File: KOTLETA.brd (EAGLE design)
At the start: 27 x 40.2 mm, 126 parts, among them CON1 CON-6P, CON2 CON-4P-JST_GH-RA, CON3 CON-4P-JST_GH-RA, IC1 STM32F105RCT6, IC2 CAT24C02, IC3 SN65HVD232D, IC4 LMR14010ADDCT, IC5 LM75BD-TSSOP8, IC6 FAN7888, IC7 ZXCT1051, IC8 3.3V, Q1 CSD18510Q5B, Q2 CSD18510Q5B, Q3 CSD18510Q5B, Q4 CSD18510Q5B, Q5 CSD18510Q5B, Q6 CSD18510Q5B, X1 24MHz

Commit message: BOM updates
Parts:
- C24, C30, C32: value 2.2nF -> 1800pF
- R13, R18, R22: value 3K9 -> 4K7
- moved PAD3 0.20 mm to (0.00, 18.7)
- moved PAD5 0.20 mm to (0.00, 16.1)
- moved PAD1 0.20 mm to (0.00, 20.5)
- moved PAD2 0.20 mm to (0.00, 19.6)
- moved PAD4 0.20 mm to (0.00, 15.2)
- moved PAD6 0.20 mm to (0.00, 17.1)

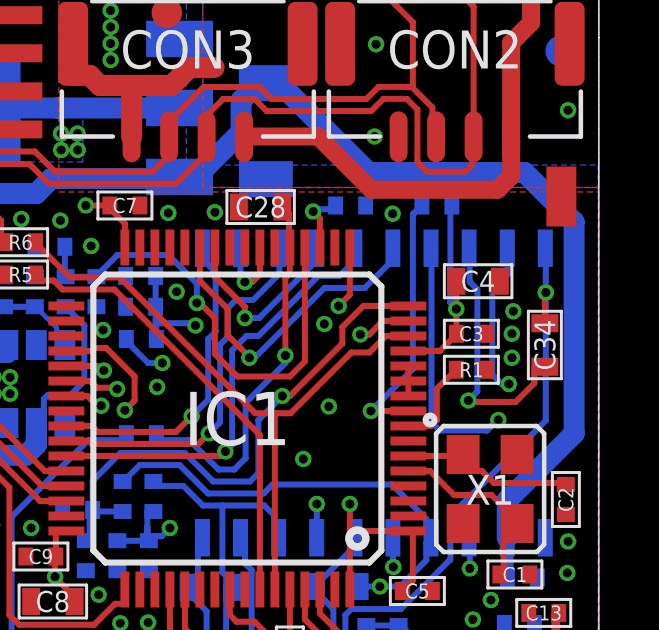
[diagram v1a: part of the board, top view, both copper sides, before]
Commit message: Its 10V5 noew. HW ID stuff also fixed
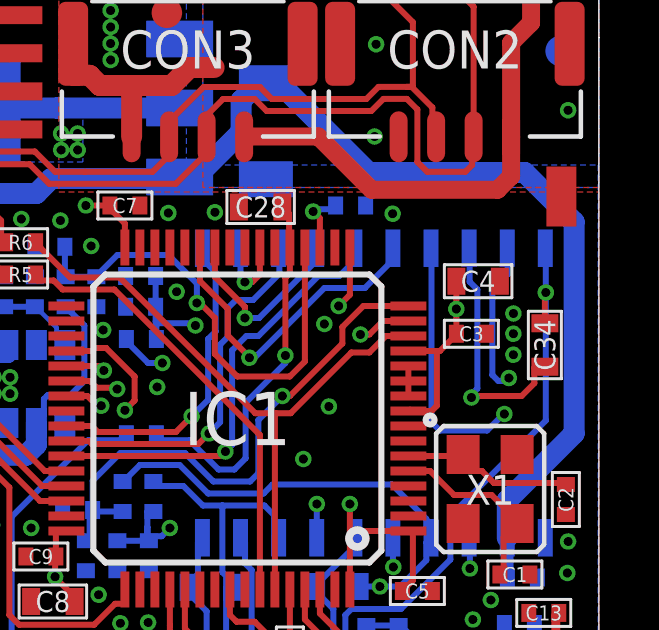
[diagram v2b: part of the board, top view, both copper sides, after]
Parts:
- removed R1, R29: 200R, R_digikey:R0402
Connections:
- removed net N$15: IC1.9, R29.1
- removed net N$9: IC1.8, R1.1
- net GND: now also IC1.8; no longer R1.2
- net VDD_3V3: now also IC1.9; no longer R29.2
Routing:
- net N$15: track 8.87 -> 0.00 mm, vias 1 -> 0
- net N$9: track 2.98 -> 0.00 mm
- net VDD_3V3: track 57.6 -> 56.9 mm

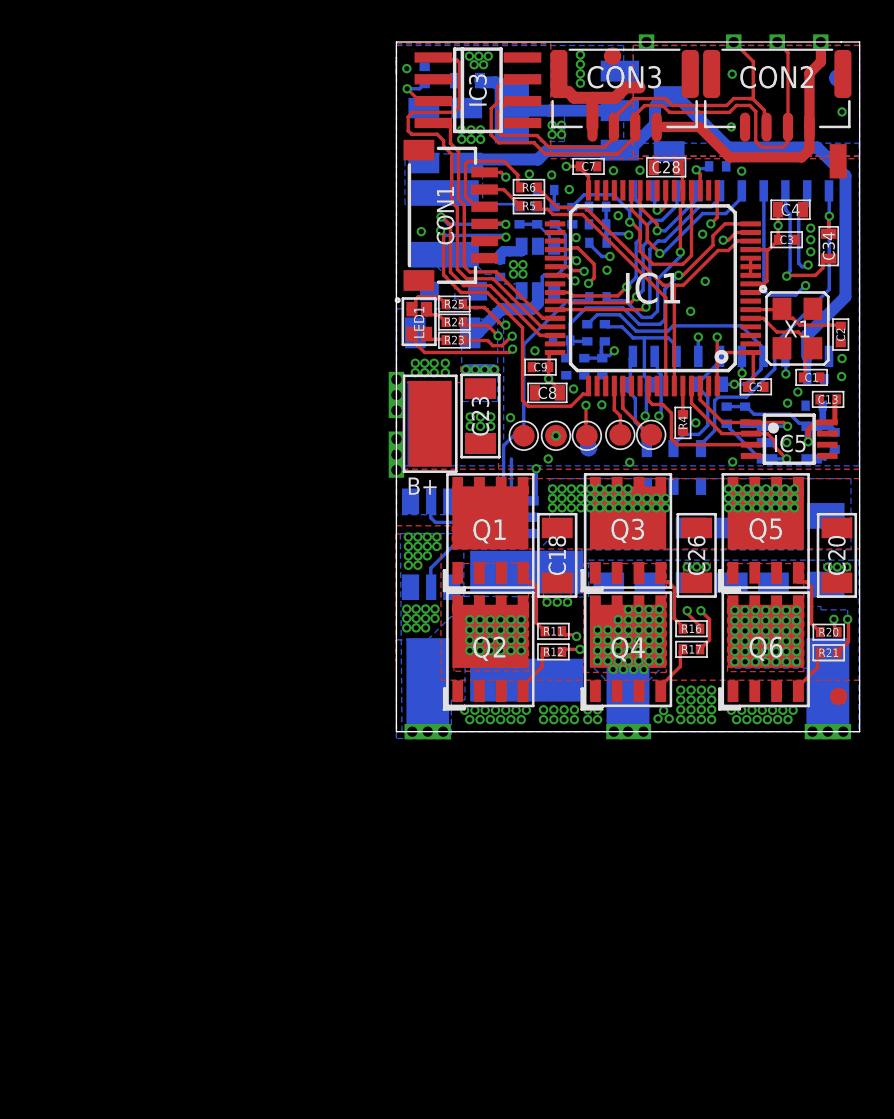
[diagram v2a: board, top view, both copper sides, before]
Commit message: pads for bulk capacitor
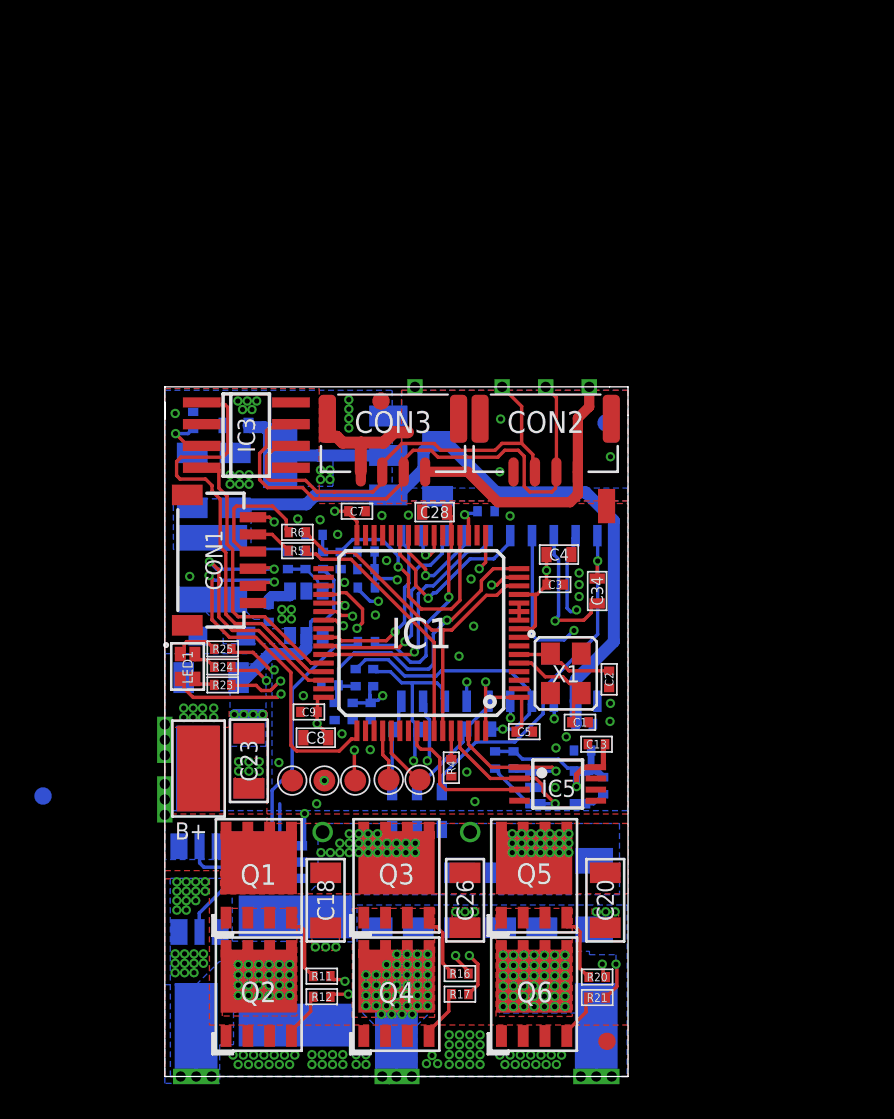
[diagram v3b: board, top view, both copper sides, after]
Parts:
- added PAD21, PAD22: PAD-HOLE-0.8, PADS:HOLE_0.8
- moved FD4 37.7 mm to (-20.6, -3.75)
- moved D5 25.1 mm to (2.65, -4.60)
- moved D4 25.0 mm to (1.20, -4.60)
- moved D3 24.9 mm to (-0.25, -4.60)
- moved C10 24.2 mm to (10.8, -1.10)
- moved C21 24.2 mm to (8.47, -9.82)
- moved C4 24.2 mm to (9.47, 10.3)
- moved C6 24.2 mm to (5.22, 12.8)
- moved FD3 24.2 mm to (12.2, 18.0)
- moved A 24.2 mm to (-11.7, -17.1)
- moved B 24.2 mm to (0.00, -17.1)
- moved B+ 24.2 mm to (-11.5, -2.15)
- moved B- 24.2 mm to (-11.6, -2.15)
- moved C1 24.2 mm to (10.7, 0.55)
- moved C11 24.2 mm to (-11.8, 18.1)
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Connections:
- net GND: now also PAD22.P$1
- net VBAT: now also PAD21.P$1
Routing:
- net FET_C_VB: track 20.1 -> 21.2 mm
- net FET_A_HO: track 22.3 -> 21.4 mm
- net FET_A_VS: track 27.9 -> 27.0 mm
- net VBAT: track 14.5 -> 15.4 mm, vias 63 -> 49
- net N$20: track 5.04 -> 5.66 mm
- net FET_A_VB: track 6.09 -> 5.50 mm
- net GND: vias 63 -> 62

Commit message: blah
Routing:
- net FET_B_VS: vias 42 -> 38
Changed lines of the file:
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@@
 <grid distance="0.025" unitdist="mm" unit="mm" style="lines" multiple="2" display="yes" altdistance="1" altunitdist="mm" altunit="mm"/>
 <layers>
-<layer number="1" name="Top" color="4" fill="1" visible="yes" active="yes"/>
+<layer number="1" name="Top" color="4" fill="1" visible="no" active="yes"/>
 <layer number="2" name="gnd" color="1" fill="3" visible="no" active="yes"/>
 <layer number="3" name="SUPPLY" color="2" fill="5" visible="no" active="yes"/>
@@
 <layer number="17" name="Pads" color="2" fill="1" visible="yes" active="yes"/>
 <layer number="18" name="Vias" color="2" fill="1" visible="yes" active="yes"/>
-<layer number="19" name="Unrouted" color="14" fill="1" visible="no" active="yes"/>
+<layer number="19" name="Unrouted" color="14" fill="1" visible="yes" active="yes"/>
 <layer number="20" name="Dimension" color="15" fill="1" visible="yes" active="yes"/>
-<layer number="21" name="tPlace" color="7" fill="1" visible="yes" active="yes"/>
+<layer number="21" name="tPlace" color="7" fill="1" visible="no" active="yes"/>
 <layer number="22" name="bPlace" color="7" fill="1" visible="no" active="yes"/>
-<layer number="23" name="tOrigins" color="15" fill="1" visible="yes" active="yes"/>
+<layer number="23" name="tOrigins" color="15" fill="1" visible="no" active="yes"/>
 <layer number="24" name="bOrigins" color="15" fill="1" visible="no" active="yes"/>
-<layer number="25" name="tNames" color="7" fill="1" visible="yes" active="yes"/>
+<layer number="25" name="tNames" color="7" fill="1" visible="no" active="yes"/>
 <layer number="26" name="bNames" color="7" fill="1" visible="no" active="yes"/>
 <layer number="27" name="tValues" color="7" fill="1" visible="no" active="yes"/>
@@
 <layer number="49" name="Reference" color="7" fill="1" visible="no" active="yes"/>
 <layer number="50" name="dxf" color="7" fill="1" visible="no" active="no"/>
-<layer number="51" name="tDocu" color="7" fill="1" visible="yes" active="yes"/>
+<layer number="51" name="tDocu" color="7" fill="1" visible="no" active="yes"/>
 <layer number="52" name="bDocu" color="7" fill="1" visible="no" active="yes"/>
 <layer number="53" name="tGND_GNDA" color="7" fill="9" visible="no" active="no"/>
@@
 <via x="1.8" y="-1.7" extent="1-16" drill="0.3"/>
 <wire x1="1.8" y1="-1.7" x2="1.925" y2="-1.575" width="0.2" layer="16"/>
-<wire x1="2.15" y1="-8.55" x2="2.15" y2="-2.325" width="0.2" layer="3"/>
-<wire x1="2.15" y1="-2.325" x2="1.8" y2="-1.975" width="0.2" layer="3"/>
-<wire x1="1.8" y1="-1.975" x2="1.8" y2="-1.7" width="0.2" layer="3"/>
-<wire x1="-1.9" y1="-9.85" x2="0.85" y2="-9.85" width="0.2" layer="3"/>
-<wire x1="0.85" y1="-9.85" x2="2.15" y2="-8.55" width="0.2" layer="3"/>
+<wire x1="2.3" y1="-8.05" x2="2.3" y2="-2.225" width="0.2" layer="3"/>
+<wire x1="2.3" y1="-2.225" x2="1.8" y2="-1.725" width="0.2" layer="3"/>
+<wire x1="1.8" y1="-1.725" x2="1.8" y2="-1.7" width="0.2" layer="3"/>
+<wire x1="-1.975" y1="-9.925" x2="0.425" y2="-9.925" width="0.2" layer="3"/>
+<wire x1="0.425" y1="-9.925" x2="2.3" y2="-8.05" width="0.2" layer="3"/>
 <wire x1="-3.85" y1="-14.25" x2="-3.65" y2="-14.45" width="0.2" layer="1"/>
-<wire x1="-1.9" y1="-9.85" x2="-2.8" y2="-10.75" width="0.2" layer="3"/>
-<wire x1="-2.8" y1="-10.75" x2="-2.8" y2="-14.35" width="0.2" layer="3"/>
-<wire x1="-2.8" y1="-14.35" x2="-3" y2="-14.55" width="0.2" layer="3"/>
+<wire x1="-1.975" y1="-9.925" x2="-2.95" y2="-10.9" width="0.2" layer="3"/>
+<wire x1="-2.95" y1="-10.9" x2="-2.95" y2="-14.5" width="0.2" layer="3"/>
+<wire x1="-2.95" y1="-14.5" x2="-3" y2="-14.55" width="0.2" layer="3"/>
 <wire x1="1.705" y1="1.624" x2="1.555" y2="1.774" width="0.2" layer="16"/>
 <wire x1="1.705" y1="1.624" x2="1.705" y2="0.92" width="0.2" layer="16"/>
@@
 <via x="-6.225" y="-15.375" extent="1-16" drill="0.3"/>
 <wire x1="0.95" y1="2.85" x2="2.35" y2="2.85" width="0.2" layer="16"/>
-<wire x1="1.725" y1="-8.375" x2="1.725" y2="-2.725" width="0.2" layer="3"/>
-<wire x1="1.725" y1="-2.725" x2="1" y2="-2" width="0.2" layer="3"/>
-<wire x1="1" y1="-2" x2="1" y2="-1.7" width="0.2" layer="3"/>
+<wire x1="1.725" y1="-7.825" x2="1.725" y2="-2.5" width="0.2" layer="3"/>
+<wire x1="1.725" y1="-2.5" x2="1" y2="-1.775" width="0.2" layer="3"/>
+<wire x1="1" y1="-1.775" x2="1" y2="-1.7" width="0.2" layer="3"/>
 <via x="1" y="-1.7" extent="1-16" drill="0.3"/>
 <wire x1="1.075" y1="0.125" x2="1.075" y2="-1.625" width="0.2" layer="16"/>
@@
 <vertex x="-9.4" y="-16.3"/>
 </polygon>
-<wire x1="1.725" y1="-8.375" x2="0.7" y2="-9.4" width="0.2" layer="3"/>
-<wire x1="0.7" y1="-9.4" x2="-3.6" y2="-9.4" width="0.2" layer="3"/>
+<wire x1="1.725" y1="-7.825" x2="0.15" y2="-9.4" width="0.2" layer="3"/>
+<wire x1="0.15" y1="-9.4" x2="-3.6" y2="-9.4" width="0.2" layer="3"/>
 <wire x1="-3.6" y1="-9.4" x2="-4.35" y2="-10.15" width="0.2" layer="3"/>
 <contactref element="Q2" pad="PAD_D"/>
@@
 <via x="-2.8" y="-15.3" extent="1-16" drill="0.3"/>
 <via x="4.1" y="2.9" extent="1-16" drill="0.3"/>
-<wire x1="2.925" y1="-8.375" x2="2.925" y2="1.725" width="0.2" layer="3"/>
-<wire x1="2.925" y1="1.725" x2="4.1" y2="2.9" width="0.2" layer="3"/>
-<wire x1="2.925" y1="-8.375" x2="1.05" y2="-10.25" width="0.2" layer="3"/>
-<wire x1="1.05" y1="-10.25" x2="-1.7" y2="-10.25" width="0.2" layer="3"/>
-<wire x1="-1.7" y1="-10.25" x2="-2.4" y2="-10.95" width="0.2" layer="3"/>
-<wire x1="-2.4" y1="-10.95" x2="-2.4" y2="-14.9" width="0.2" layer="3"/>
+<wire x1="2.825" y1="-8.325" x2="2.825" y2="1.625" width="0.2" layer="3"/>
+<wire x1="2.825" y1="1.625" x2="4.1" y2="2.9" width="0.2" layer="3"/>
+<wire x1="2.825" y1="-8.325" x2="0.725" y2="-10.425" width="0.2" layer="3"/>
+<wire x1="0.725" y1="-10.425" x2="-1.475" y2="-10.425" width="0.2" layer="3"/>
+<wire x1="-1.475" y1="-10.425" x2="-2.4" y2="-11.35" width="0.2" layer="3"/>
+<wire x1="-2.4" y1="-11.35" x2="-2.4" y2="-14.9" width="0.2" layer="3"/>
 <wire x1="-2.4" y1="-14.9" x2="-2.8" y2="-15.3" width="0.2" layer="3"/>
 <wire x1="-2.8" y1="-15.3" x2="-3.7" y2="-15.3" width="0.2" layer="1"/>
@@
 <via x="0.625" y="-15.975" extent="1-16" drill="0.3"/>
 <via x="1.225" y="-15.975" extent="1-16" drill="0.3"/>
-<via x="-0.875" y="-16.475" extent="1-16" drill="0.3"/>
-<via x="-0.275" y="-16.475" extent="1-16" drill="0.3"/>
-<via x="0.325" y="-16.475" extent="1-16" drill="0.3"/>
-<via x="0.925" y="-16.475" extent="1-16" drill="0.3"/>
 <wire x1="7.75066875" y1="1.92833125" x2="7.75066875" y2="2.39933125" width="0.2" layer="16"/>
 <wire x1="7.75066875" y1="1.92833125" x2="7.905" y2="1.774" width="0.2" layer="16"/>
@@
 <wire x1="8.55" y1="2.5" x2="11.731" y2="5.681" width="0.2" layer="16"/>
 <wire x1="2.65" y1="-3.5" x2="2.75" y2="-3.6" width="0.2" layer="16"/>
-<wire x1="6.9" y1="-0.6" x2="4.636825" y2="-0.6" width="0.2" layer="16"/>
+<wire x1="6.9" y1="-0.6" x2="5.025" y2="-0.6" width="0.2" layer="16"/>
+<wire x1="5.025" y1="-0.6" x2="4.911825" y2="-0.6" width="0.2" layer="16"/>
 <wire x1="6.9" y1="-0.6" x2="8.55" y2="1.05" width="0.2" layer="16"/>
 <wire x1="11.7" y1="8.925" x2="11.7" y2="9.919" width="0.2" layer="1"/>
@@
 <wire x1="11.731" y1="9.95" x2="11.731" y2="11.41" width="0.2" layer="16"/>
 <wire x1="11.731" y1="11.41" x2="11.715" y2="11.426" width="0.2" layer="16"/>
-<wire x1="4.636825" y1="-0.6" x2="2.65" y2="-2.586825" width="0.2" layer="16"/>
-<wire x1="2.65" y1="-2.586825" x2="2.65" y2="-3.5" width="0.2" layer="16"/>
+<wire x1="2.85" y1="-3.3" x2="2.85" y2="-2.661825" width="0.2" layer="16"/>
+<wire x1="2.85" y1="-3.3" x2="2.65" y2="-3.5" width="0.2" layer="16"/>
+<wire x1="2.85" y1="-2.661825" x2="4.911825" y2="-0.6" width="0.2" layer="16"/>
+<wire x1="4.911825" y1="-0.6" x2="5.025" y2="-0.6" width="0.2" layer="16"/>
 </signal>
 <signal name="USART1_TX">
@@
 <wire x1="7.15" y1="4.5" x2="8.925" y2="4.5" width="0.2" layer="1"/>
 <wire x1="8.925" y1="4.5" x2="8.975" y2="4.55" width="0.2" layer="1"/>
-<wire x1="12.4" y1="3.55" x2="12.35" y2="3.6" width="0.2" layer="1"/>
 <wire x1="12.4" y1="3.55" x2="10.0632375" y2="3.55" width="0.2" layer="1"/>
 <wire x1="10.0632375" y1="3.55" x2="9.6132375" y2="4" width="0.2" layer="1"/>

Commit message: notes
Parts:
- removed PAD21, PAD22: PAD-HOLE-0.8, PADS:HOLE_0.8
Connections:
- net GND: no longer PAD22.P$1
- net VBAT: no longer PAD21.P$1
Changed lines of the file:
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@@
 <grid distance="0.025" unitdist="mm" unit="mm" style="lines" multiple="2" display="yes" altdistance="1" altunitdist="mm" altunit="mm"/>
 <layers>
-<layer number="1" name="Top" color="4" fill="1" visible="no" active="yes"/>
+<layer number="1" name="Top" color="4" fill="1" visible="yes" active="yes"/>
 <layer number="2" name="gnd" color="1" fill="3" visible="no" active="yes"/>
 <layer number="3" name="SUPPLY" color="2" fill="5" visible="no" active="yes"/>
@@
 <layer number="19" name="Unrouted" color="14" fill="1" visible="yes" active="yes"/>
 <layer number="20" name="Dimension" color="15" fill="1" visible="yes" active="yes"/>
-<layer number="21" name="tPlace" color="7" fill="1" visible="no" active="yes"/>
+<layer number="21" name="tPlace" color="7" fill="1" visible="yes" active="yes"/>
 <layer number="22" name="bPlace" color="7" fill="1" visible="no" active="yes"/>
-<layer number="23" name="tOrigins" color="15" fill="1" visible="no" active="yes"/>
+<layer number="23" name="tOrigins" color="15" fill="1" visible="yes" active="yes"/>
 <layer number="24" name="bOrigins" color="15" fill="1" visible="no" active="yes"/>
-<layer number="25" name="tNames" color="7" fill="1" visible="no" active="yes"/>
+<layer number="25" name="tNames" color="7" fill="1" visible="yes" active="yes"/>
 <layer number="26" name="bNames" color="7" fill="1" visible="no" active="yes"/>
 <layer number="27" name="tValues" color="7" fill="1" visible="no" active="yes"/>
@@
 <layer number="49" name="Reference" color="7" fill="1" visible="no" active="yes"/>
 <layer number="50" name="dxf" color="7" fill="1" visible="no" active="no"/>
-<layer number="51" name="tDocu" color="7" fill="1" visible="no" active="yes"/>
+<layer number="51" name="tDocu" color="7" fill="1" visible="yes" active="yes"/>
 <layer number="52" name="bDocu" color="7" fill="1" visible="no" active="yes"/>
 <layer number="53" name="tGND_GNDA" color="7" fill="9" visible="no" active="no"/>
@@
 <attribute name="VALUE" x="-6.2" y="9.975" size="0.5" layer="28" font="vector" ratio="15" rot="MR270" align="center"/>
 </element>
-<element name="PAD21" library="PADS" library_urn="urn:adsk.eagle:library:3188696" package="HOLE_0.8" value="PAD-HOLE-0.8" x="4.3" y="-5.85" smashed="yes" rot="MR90"/>
-<element name="PAD22" library="PADS" library_urn="urn:adsk.eagle:library:3188696" package="HOLE_0.8" value="PAD-HOLE-0.8" x="-4.3" y="-5.85" smashed="yes" rot="R90"/>
 </elements>
 <signals>
@@
 </polygon>
 <wire x1="-13.5" y1="0.425" x2="-13.5" y2="-0.475" width="0.2" layer="1"/>
-<contactref element="PAD21" pad="P$1"/>
 </signal>
 <signal name="FET_A_L">
@@
 <via x="-2.775" y="17.7" extent="1-16" drill="0.3" diameter="0.55"/>
 <contactref element="IC1" pad="8"/>
-<contactref element="PAD22" pad="P$1"/>
 </signal>
 <signal name="SENSE_B">
